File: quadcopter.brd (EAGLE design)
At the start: 127.2 x 127.2 mm, 77 parts, among them J1 AVR_SPI_PRG_6NS, J3 HEADER-0.1IN-2POS-FEMALE, J4 HEADER-0.1IN-2POS-FEMALE, J5 HEADER-0.1IN-2POS-FEMALE, J6 HEADER-0.1IN-2POS-FEMALE, J8 HEADER-0.1IN-2POS-FEMALE, SW1 PUSHBUTTON_SMD-VERTICAL, SW2 PUSHBUTTON_SMD-VERTICAL, U1 ATMEGA128RFA1

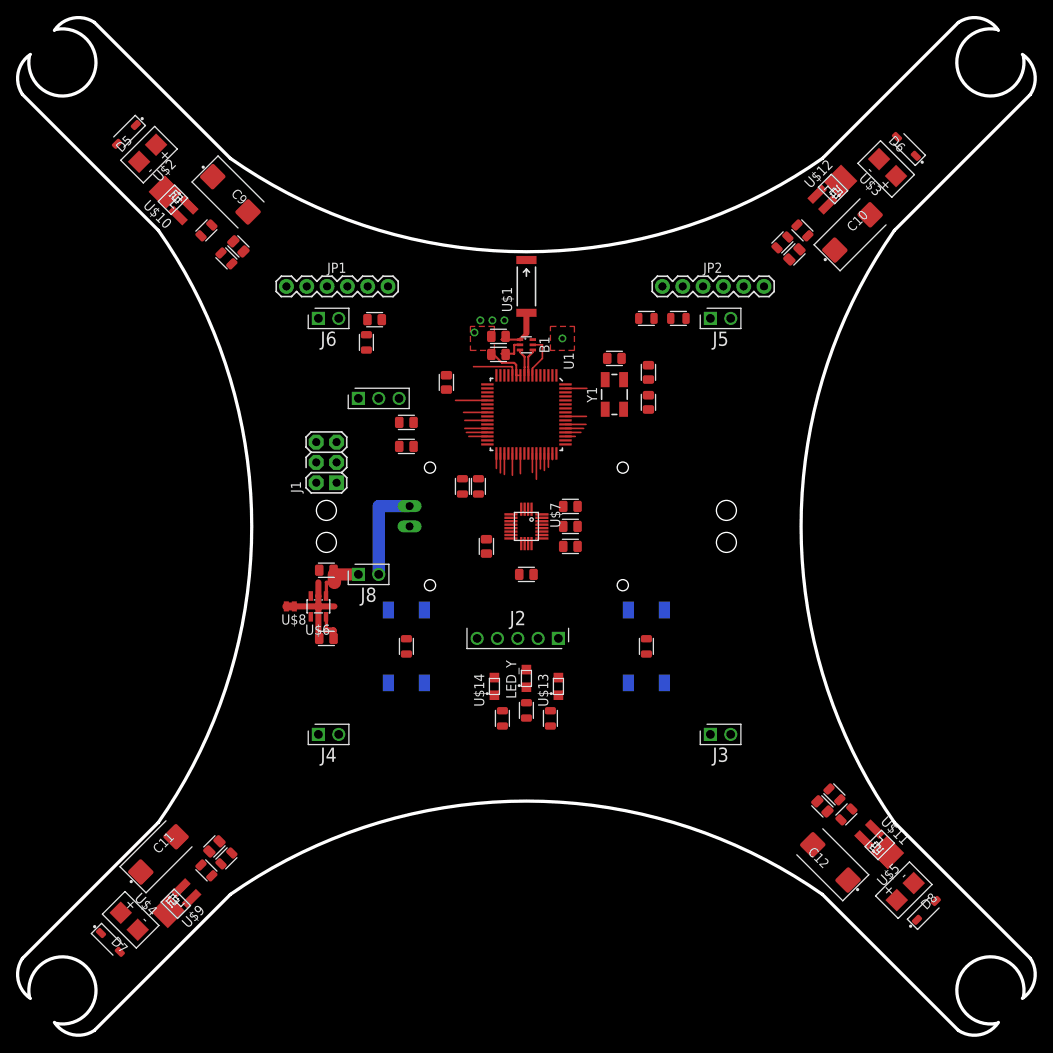
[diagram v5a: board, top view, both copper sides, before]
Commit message: Manually routed motors
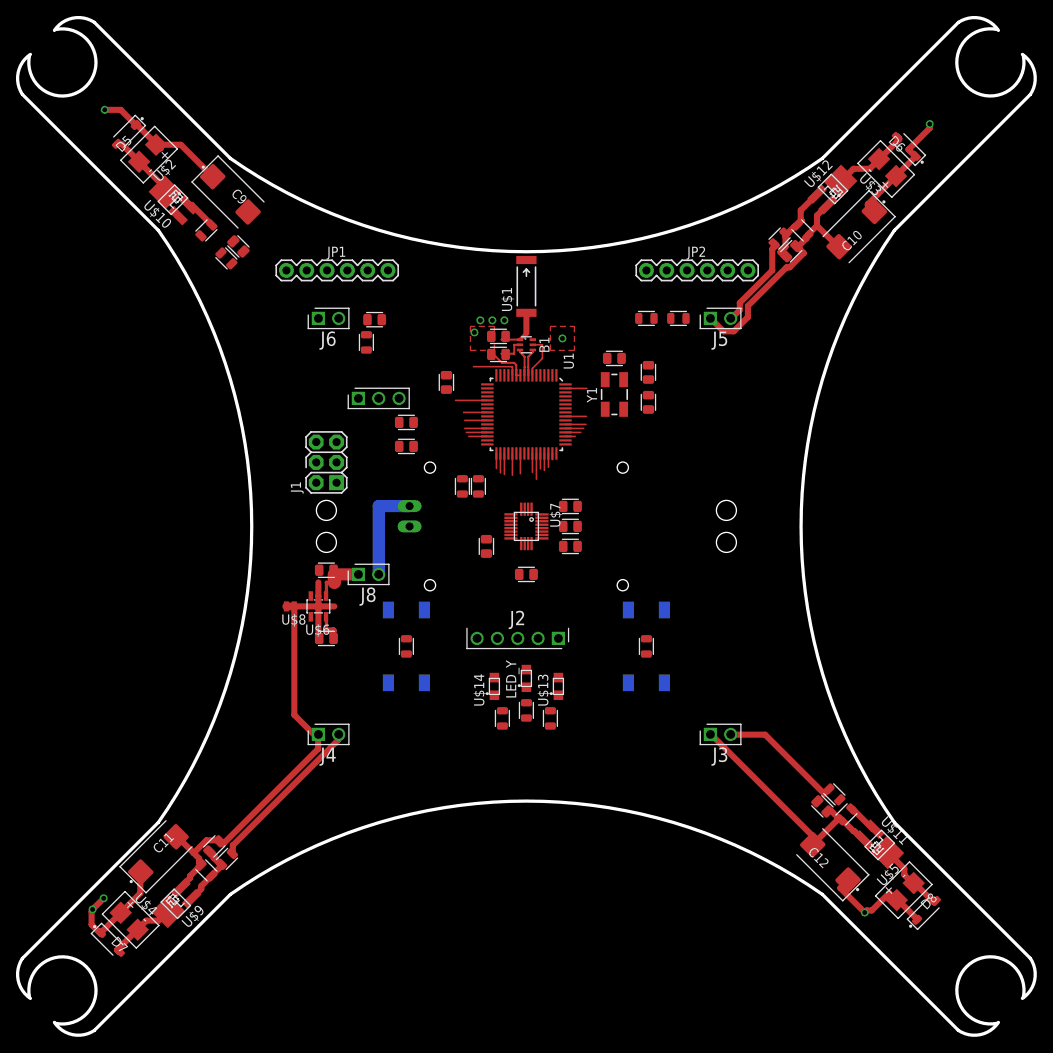
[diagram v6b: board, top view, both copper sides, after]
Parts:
- moved JP2 2.83 mm to (15.0, 32.0)
- moved JP1 2.00 mm to (-30.0, 32.0)
- moved C10 0.68 mm to (41.3, 37.2), turned to 225 degrees
- moved R4 0.60 mm to (31.6, 36.0)
- moved C20 0.57 mm to (33.1, 34.4)
- moved R8 0.09 mm to (-37.4, -41.6), turned to 225 degrees
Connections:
- net N$12: now also R7.1
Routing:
- net BAT_GND: track 0.00 -> 113.3 mm
- net V_BAT: track 14.8 -> 78.6 mm, vias 0 -> 5
- net M2_CTL: track 2.32 -> 22.7 mm
- net M1_CTL: track 0.00 -> 15.6 mm
- net M3_CTL: track 2.62 -> 14.7 mm
- net N$8: track 0.00 -> 10.7 mm
- net FLYBACK2: track 0.00 -> 10.1 mm
- net N$7: track 0.00 -> 9.78 mm
- net FLYBACK4: track 0.00 -> 9.12 mm
- net FLYBACK3: track 0.00 -> 8.89 mm
- net N$11: track 0.00 -> 8.51 mm
- net N$13: track 0.00 -> 3.92 mm

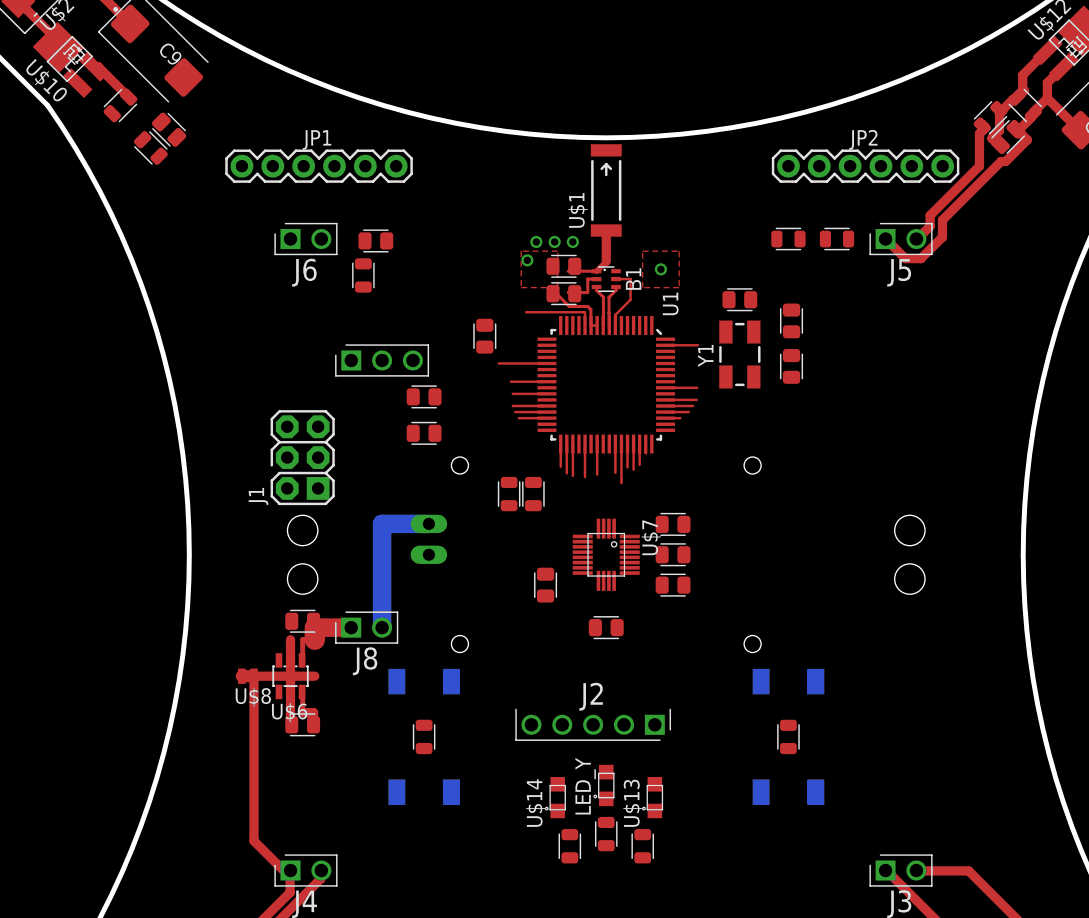
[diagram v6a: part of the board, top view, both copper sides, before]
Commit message: More manual routing
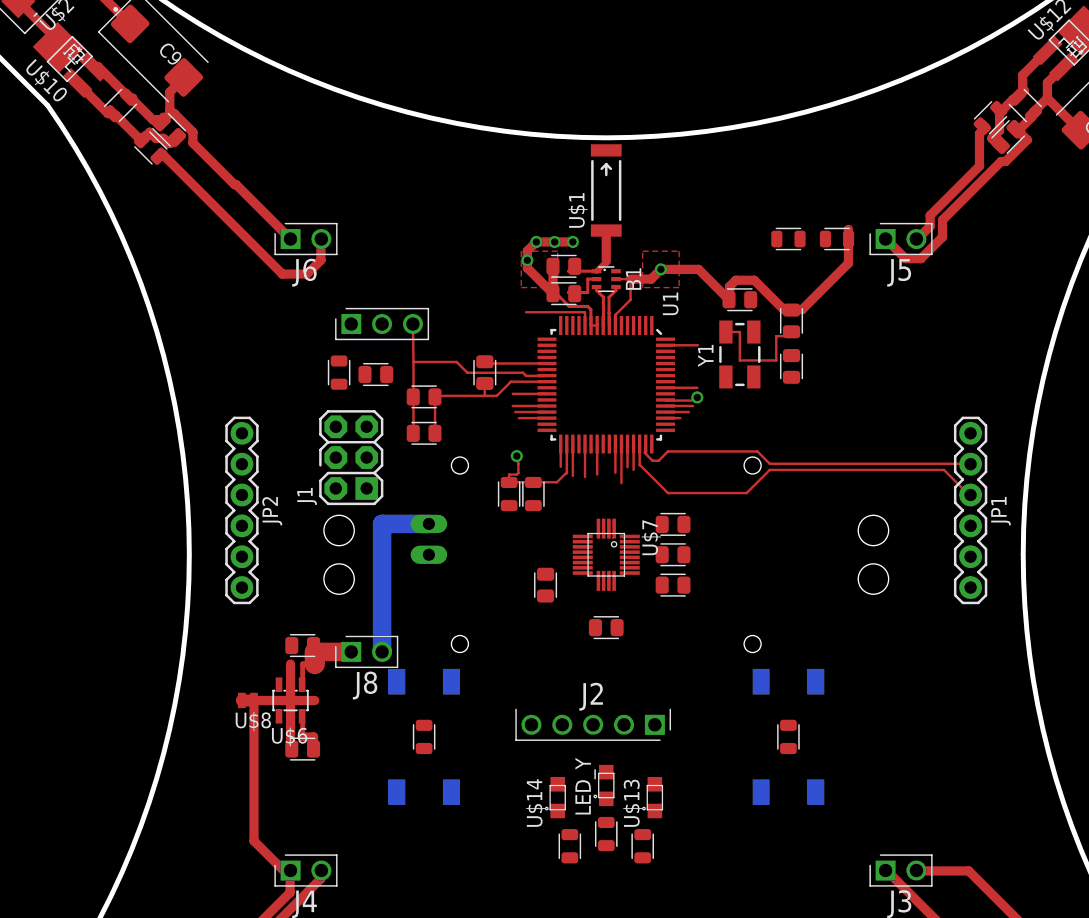
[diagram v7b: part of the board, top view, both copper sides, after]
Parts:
- moved JP1 63.9 mm to (30.0, 10.0), turned to 270 degrees
- moved JP2 50.1 mm to (-30.0, 10.0), turned to 270 degrees
- moved C5 11.0 mm to (-19.0, 14.8)
- moved R3 8.25 mm to (-22.0, 15.0), turned to 90 degrees
- moved J1 4.00 mm to (-21.0, 8.00)
- moved C24 3.00 mm to (-10.0, 15.0)
- moved J7 3.00 mm to (-21.0, 19.0)
- moved C16 2.00 mm to (-25.0, -7.48)
- moved C17 2.00 mm to (-25.0, -16.0)
- moved J8 2.00 mm to (-21.0, -8.00)
- moved U$6 2.00 mm to (-26.0, -12.0)
- moved U$8 2.00 mm to (-29.5, -12.0)
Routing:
- net GND: track 32.7 -> 80.2 mm
- net RX0: track 1.72 -> 31.7 mm
- net VCC: track 10.5 -> 39.1 mm, vias 0 -> 2
- net TX0: track 0.77 -> 29.3 mm
- net BAT_GND: track 113.3 -> 134.1 mm
- net M4_CTL: track 0.00 -> 19.7 mm
- net N$12: track 0.00 -> 10.9 mm
- net N$15: track 0.00 -> 10.1 mm
- net N$10: track 12.4 -> 14.4 mm
- net V_BAT: track 78.6 -> 80.2 mm
- net N$20: track 3.97 -> 5.26 mm

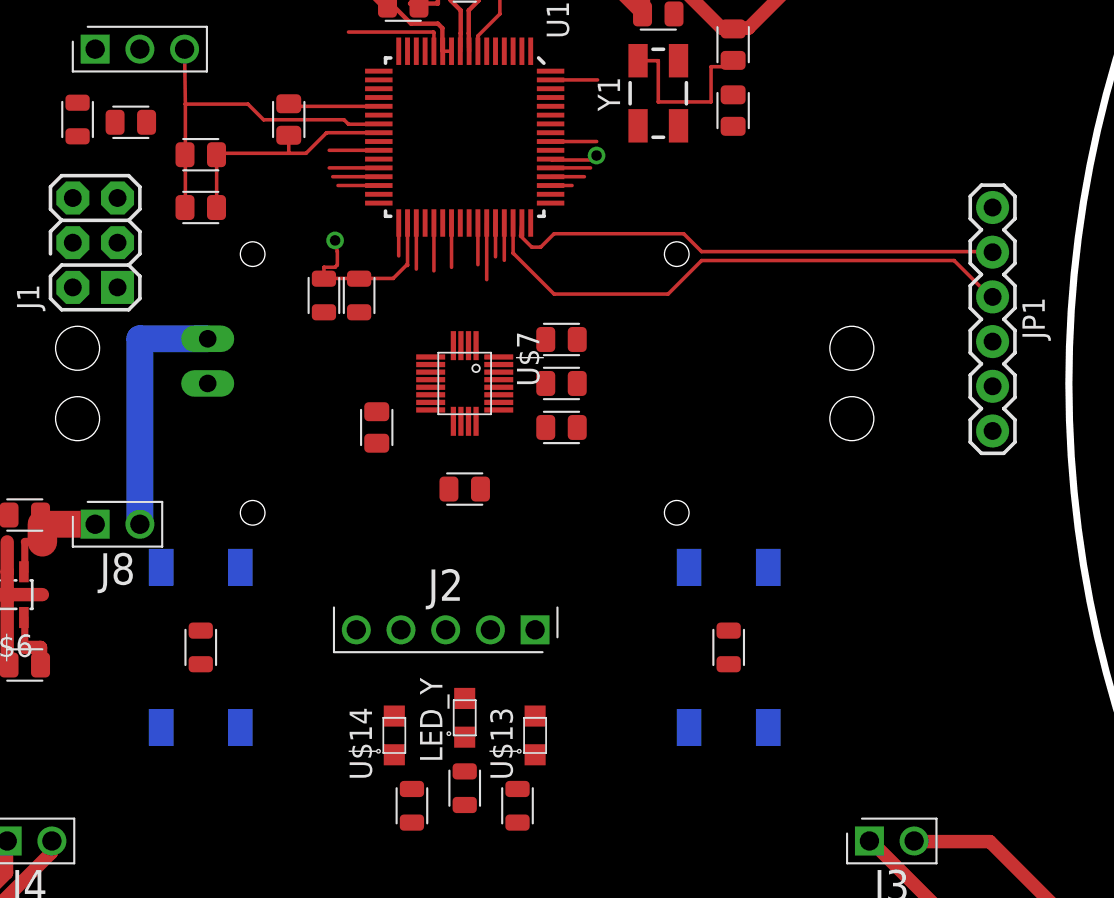
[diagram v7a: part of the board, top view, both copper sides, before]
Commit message: too much manual routing
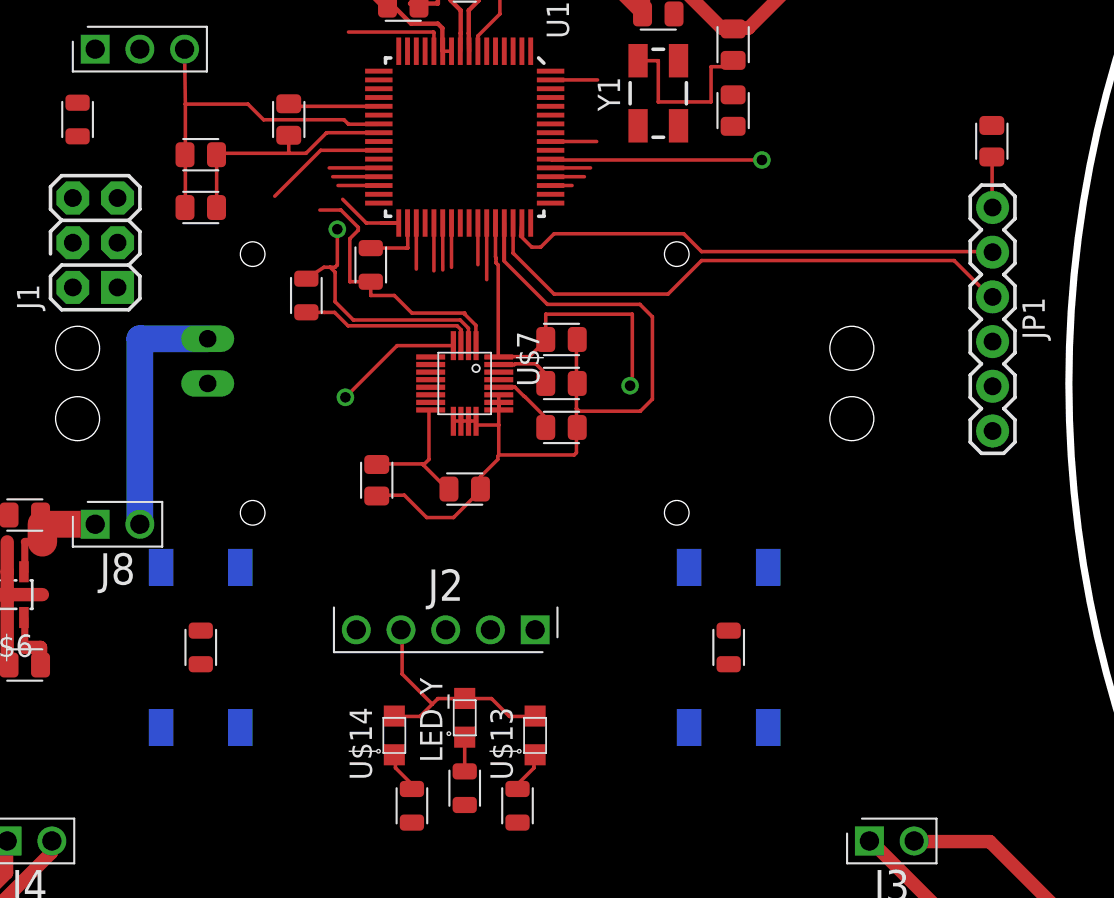
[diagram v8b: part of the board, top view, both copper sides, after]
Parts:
- moved C5 48.9 mm to (30.0, 13.8), turned to 270 degrees
- moved C6 3.00 mm to (-5.00, -5.50)
- moved R14 1.86 mm to (-5.34, 6.74)
- moved R18 1.00 mm to (-9.00, 5.00)
- turned C14 to 0 degrees
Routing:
- net GND: track 80.2 -> 145.4 mm
- net VCC: track 39.1 -> 91.7 mm, vias 2 -> 4
- net SCL: track 0.00 -> 15.7 mm
- net SDA: track 2.82 -> 17.1 mm
- net N$14: track 0.00 -> 3.94 mm
- net N$9: track 0.00 -> 3.48 mm
- net N$1: track 0.00 -> 2.89 mm
- net MOSI: track 0.00 -> 2.67 mm
- net N$6: track 0.00 -> 2.66 mm
- net N$5: track 0.00 -> 2.66 mm
- net N$18: track 0.00 -> 1.95 mm
